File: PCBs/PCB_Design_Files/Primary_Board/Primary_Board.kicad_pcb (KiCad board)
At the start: 4 copper layers, 40.3 x 57.1 mm, 128 parts, among them J1 Conn_FFC_8pin, J2 Conn_01x08_Pin, U1 OPA381, U10 TMUX1133PWR, U11 MCP6561T-E/OT, U12 TMUX1133PWR, U13 OPA320SAIDBVR, U14 AD5621AKSZ, U15 TMUX1133PWR, U2 TLV9002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

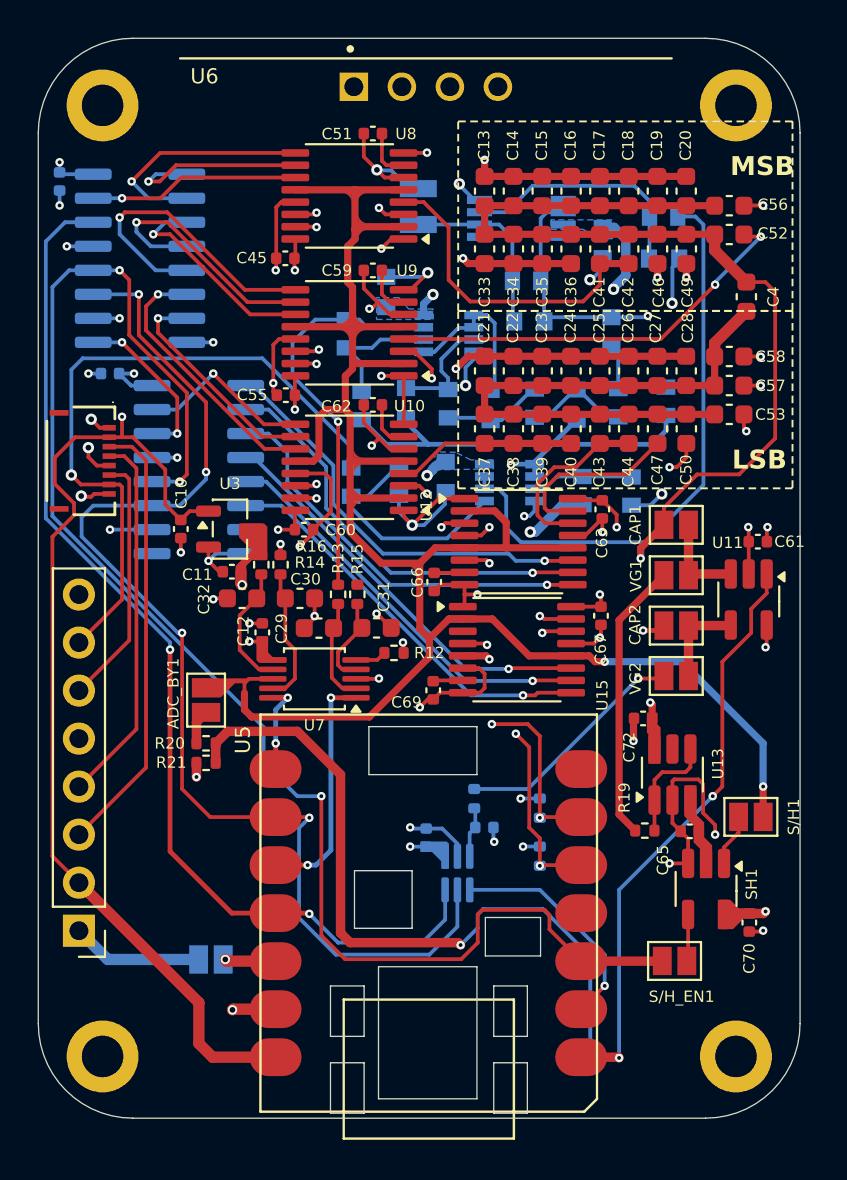
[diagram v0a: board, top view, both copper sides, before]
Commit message: updated esp library, primary board connector
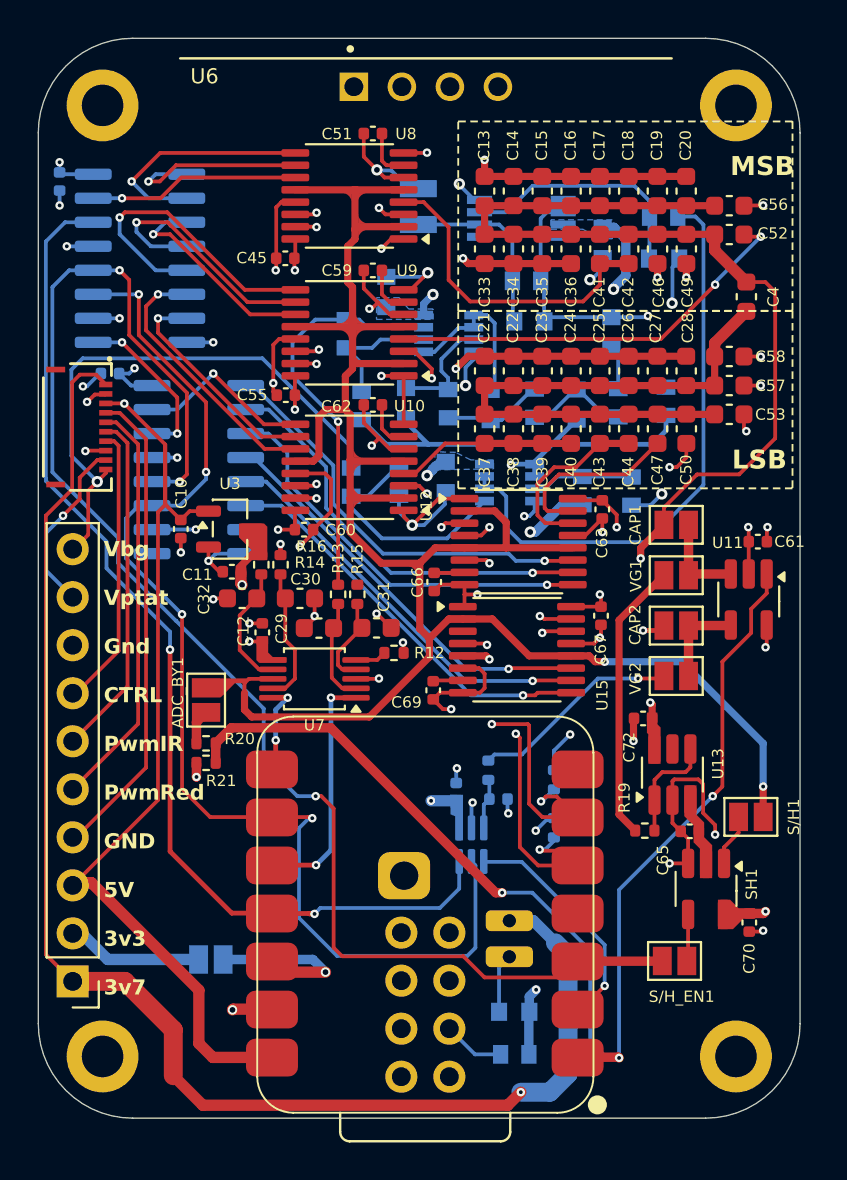
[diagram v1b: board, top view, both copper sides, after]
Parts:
- removed J1: Conn_FFC_8pin, Project Footprints:Conn_FFC_8pin
- removed J2: Conn_01x08_Pin, Connector_PinHeader_2.54mm:PinHeader_1x08_P2.54mm_Vertical
- removed U5: MOUDLE-SEEEDUINO-XIAO-ESP32C3, Project Footprints:XIAO_ESP32S3_MODULE
- added C73: 100n, Project Footprints:0603_capacitor, B.Cu at (151.2, 124.7)
- added J3: 5034801000, Project Footprints:Conn_FFC_10pin, F.Cu at (128.1, 93.8)
- added J4: Conn_01x10_Pin, Connector_PinHeader_2.54mm:PinHeader_1x10_P2.54mm_Vertical, F.Cu at (127.8, 123.1)
- added R24: 10k, Project Footprints:0603_resistor, B.Cu at (151.2, 126.9)
- added U16: XIAO-ESP32-S3-SMD, Project Footprints:XIAO-ESP32-S3-SMD, F.Cu at (155.4, 109.0)
- moved C64 2.88 mm to (148.1, 113.1)
- moved R18 1.68 mm to (149.8, 111.9)
- moved R22 1.68 mm to (153.3, 112.4)
- moved R23 1.68 mm to (153.3, 115.0)
- moved C71 1.68 mm to (150.3, 113.4)
- moved U14 1.68 mm to (148.9, 115.8)
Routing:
- net +3V7: track 0.00 -> 76.2 mm, vias 0 -> 1
- net GND: track 123.6 -> 148.9 mm
- net /OP_CTRL: track 0.00 -> 14.6 mm
- net /ADC/ADC_OUT: track 70.2 -> 63.6 mm
- net /V_bandgap: track 35.7 -> 29.6 mm
- net Net-(ESP_3V3-A): track 2.70 -> 8.57 mm
- net +3V3: track 43.6 -> 49.0 mm, vias 19 -> 20
- net /V_ptat: track 13.4 -> 9.40 mm, vias 0 -> 1
- net Net-(U16-GPIO5_A4_D4_SDA): track 60.3 -> 63.8 mm
- net Net-(U16-GPIO6_A5_D5_SCL): track 57.0 -> 60.3 mm
- net Net-(U16-CHIP_EN): track 0.00 -> 3.28 mm
- net /ADC/LATCH: track 81.2 -> 79.3 mm
- net /PWM_Red: track 23.5 -> 21.9 mm
- net /PWM_IR: track 19.8 -> 18.4 mm
- net /ADC/DAC_OUT: track 12.5 -> 11.1 mm
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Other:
- outline, holes or cut-outs redrawn
- board text added: "Vbg Vptat Gnd CTRL PwmIR PwmRed GND 5V 3v3 3v7"
- board text removed: "Gnd Vbandgap Vptat Gnd PwmIR PwmRed 5V 3v3"

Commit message: updated mcu pins
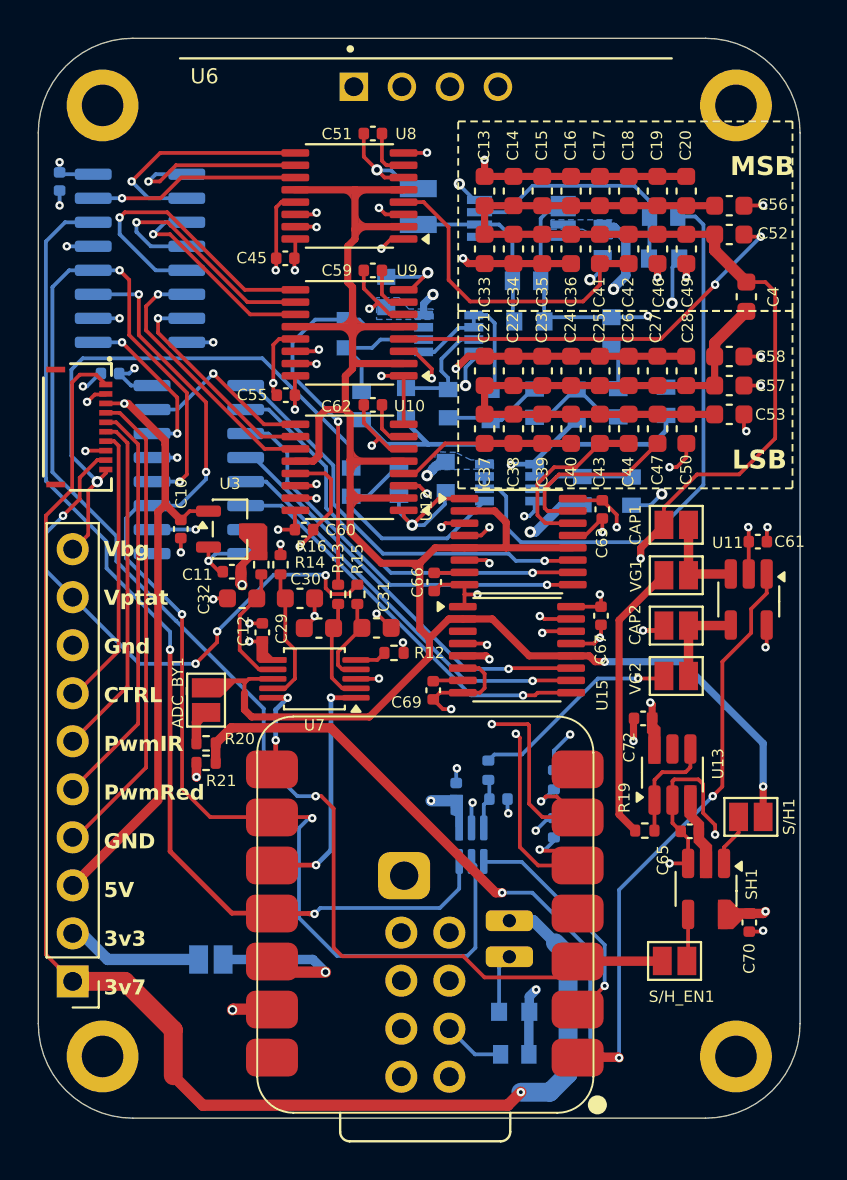
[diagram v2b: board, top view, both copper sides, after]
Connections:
- R15 pad 1: /ADC/ADC_Input3 -> /V_ptat
- U16 pad 14: +5V -> unconnected-(U16-VBUS-Pad14)
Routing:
- net /V_ptat: track 9.40 -> 29.4 mm, vias 1 -> 4
- net +5V: track 76.2 -> 60.4 mm

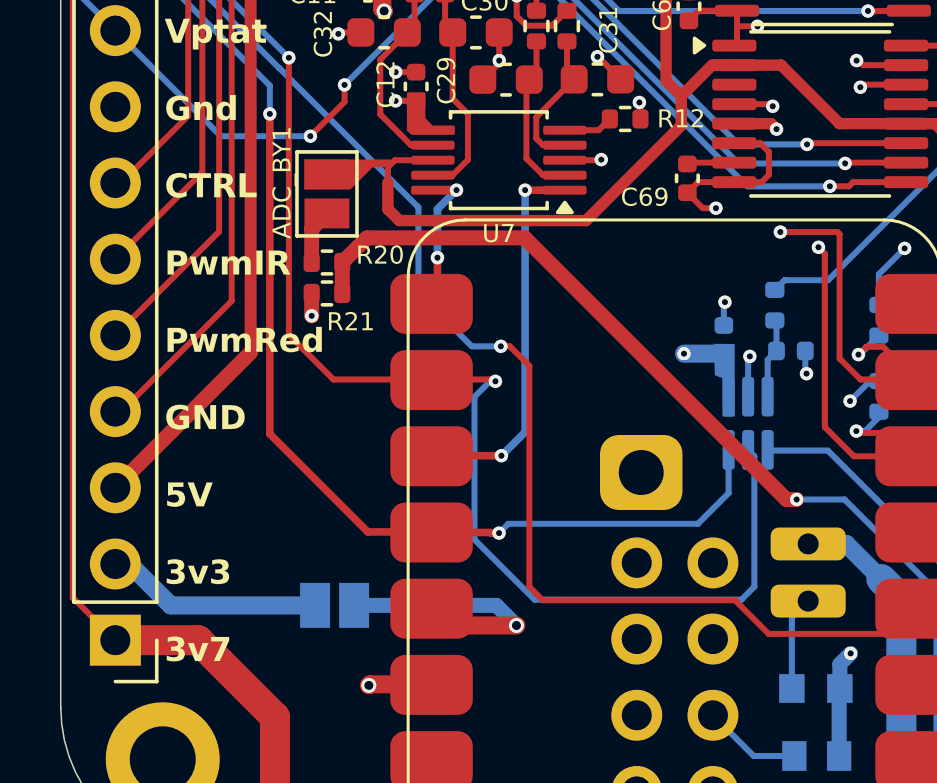
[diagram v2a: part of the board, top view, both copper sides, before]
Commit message: routed LED driver gpio on primary board
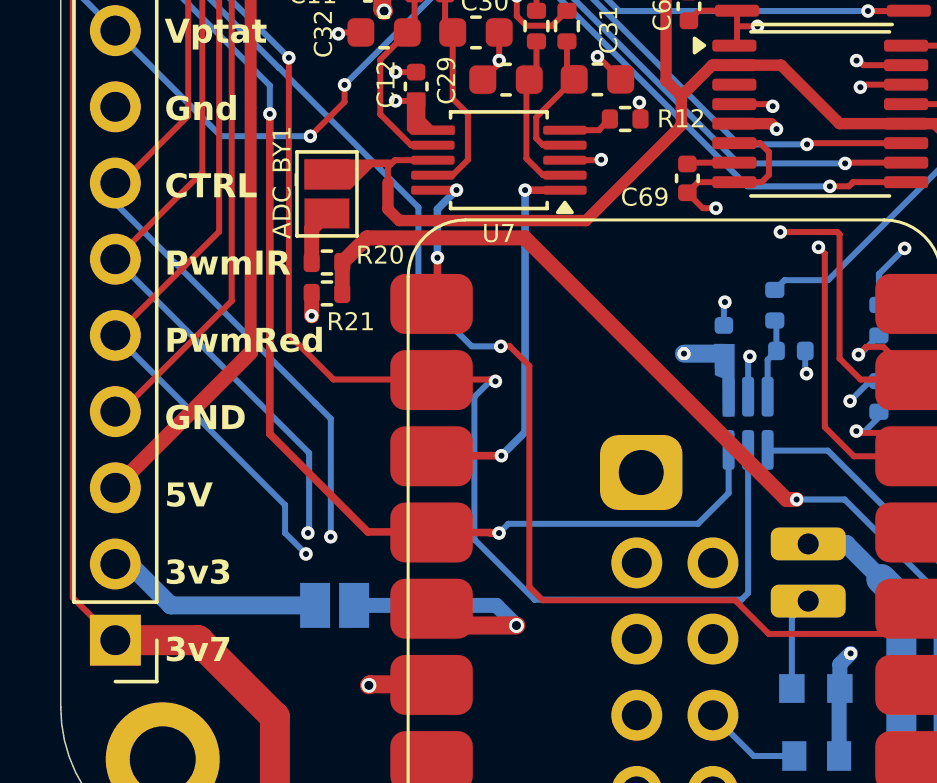
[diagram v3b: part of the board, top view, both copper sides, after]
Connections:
- U16 pad 20: unconnected-(U16-GPIO39_MTCK-Pad20) -> /OP_CTRL
- U16 pad 21: unconnected-(U16-GPIO19_USB_DN-Pad21) -> /PWM_Red
- U16 pad 22: unconnected-(U16-GPIO20_USB_DP-Pad22) -> /PWM_IR
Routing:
- net /PWM_Red: track 21.9 -> 49.8 mm, vias 0 -> 1
- net /OP_CTRL: track 14.6 -> 41.0 mm, vias 0 -> 1
- net /PWM_IR: track 18.4 -> 42.1 mm, vias 0 -> 1
